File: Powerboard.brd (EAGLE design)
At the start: 87.5 x 150 mm, 9 parts

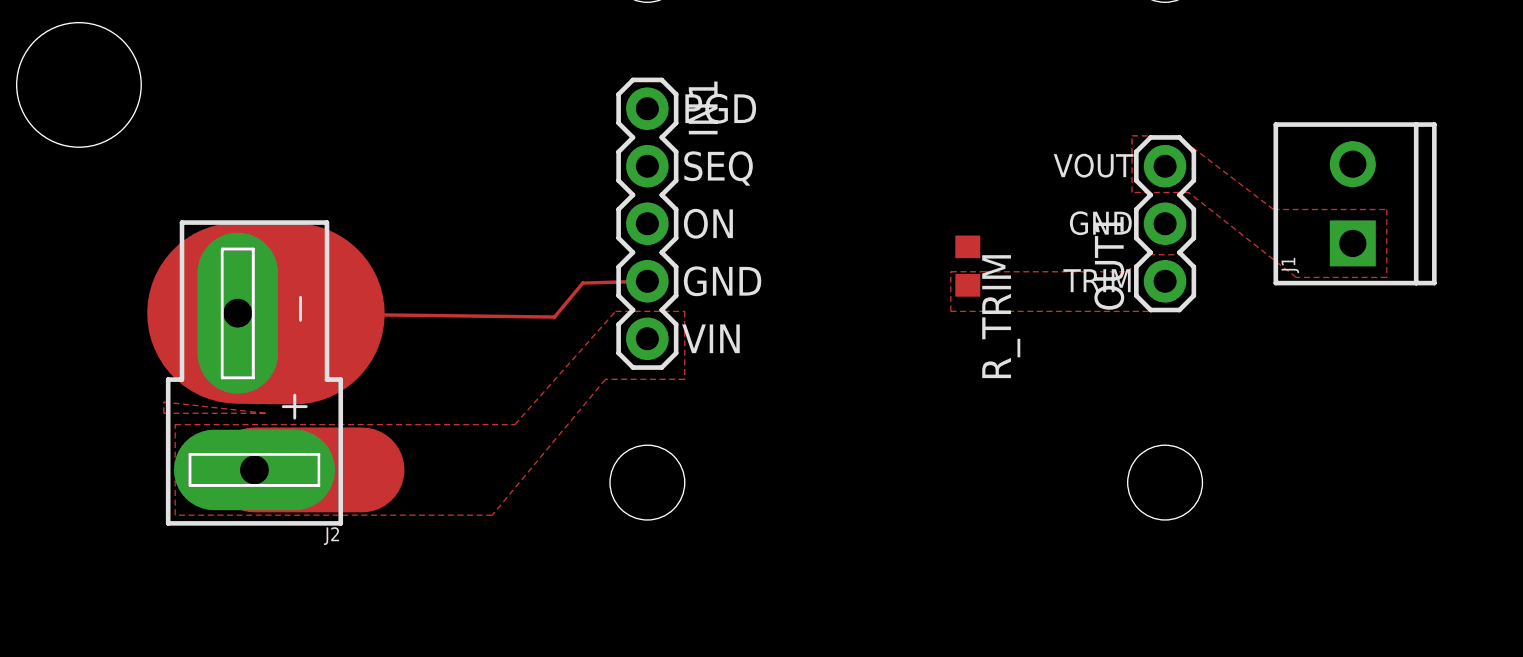
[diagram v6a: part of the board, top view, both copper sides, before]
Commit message: Rewire Powerboard
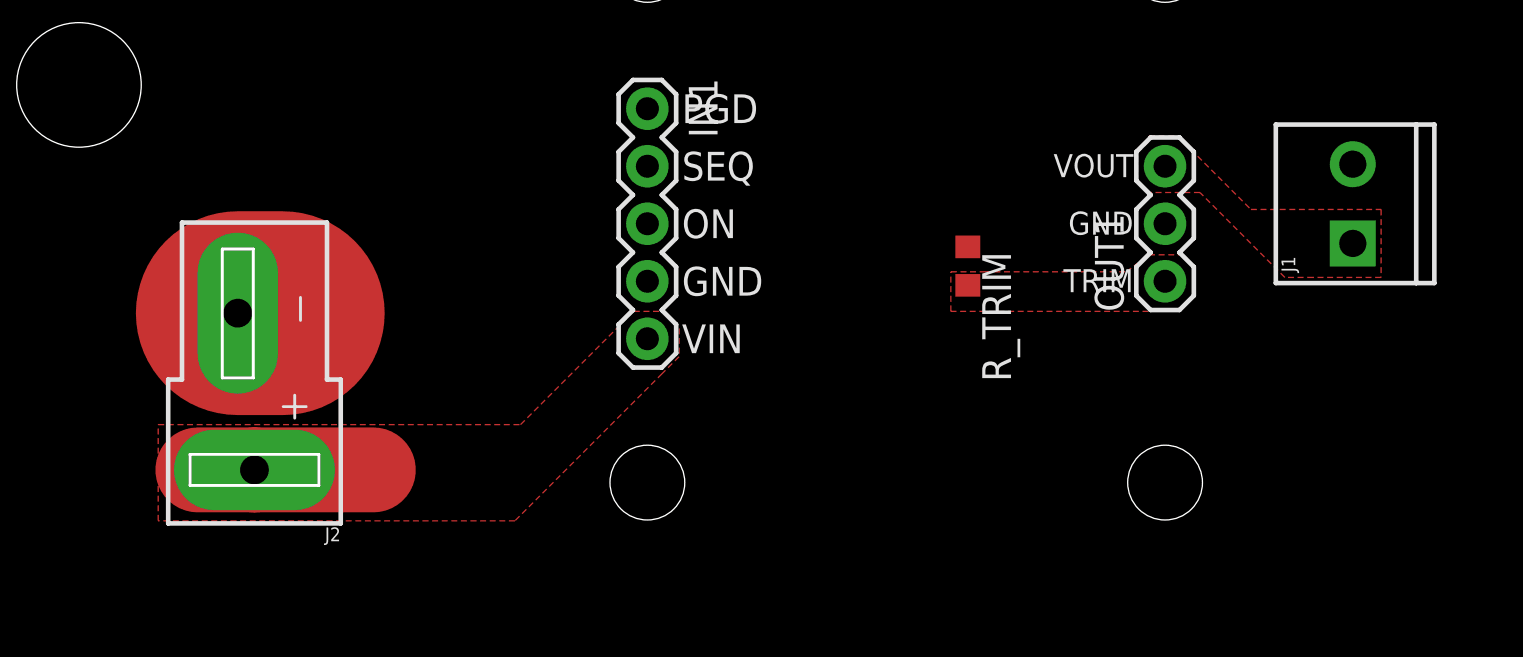
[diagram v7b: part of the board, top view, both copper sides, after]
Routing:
- net GND: track 18.8 -> 2.52 mm
- net VIN: track 4.75 -> 7.75 mm
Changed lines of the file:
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@@
 <?xml version="1.0" encoding="utf-8"?>
 <!DOCTYPE eagle SYSTEM "eagle.dtd">
-<eagle version="9.3.0">
+<eagle version="9.1.3">
 <drawing>
 <settings>
@@
 <hole x="77.75" y="140" drill="5.5"/>
 <dimension x1="77.75" y1="142.75" x2="77.75" y2="137.25" x3="97" y3="140" textsize="1.778" layer="47" dtype="diameter"/>
-<dimension x1="78" y1="140" x2="10" y2="140" x3="44" y3="169" textsize="1.778" layer="47" dtype="diameter"/>
+<dimension x1="78" y1="140" x2="10" y2="140" x3="44" y3="168.75" textsize="1.778" layer="47" dtype="diameter"/>
 <dimension x1="10" y1="9" x2="10" y2="139" x3="-10" y3="74" textsize="1.778" layer="47" dtype="diameter"/>
 <dimension x1="26" y1="150" x2="26" y2="0" x3="-15" y3="75" textsize="1.778" layer="47"/>
@@
 <contactref element="J2" pad="-"/>
 <contactref element="J1" pad="2"/>
-<polygon width="0.1524" layer="1" thermals="no">
-<vertex x="13.5" y="126"/>
-<vertex x="18" y="125.5"/>
-<vertex x="13.5" y="125.5"/>
-</polygon>
 <polygon width="0.1524" layer="1" thermals="no" rank="6">
 <vertex x="0" y="150"/>
@@
 <vertex x="87.5" y="150"/>
 </polygon>
-<wire x1="16.7634" y1="129.9215" x2="19.251728125" y2="129.8909875" width="8" layer="1"/>
-<wire x1="19.251728125" y1="129.8909875" x2="30.75" y2="129.75" width="0.1524" layer="1"/>
-<wire x1="30.75" y1="129.75" x2="32" y2="131.25" width="0.1524" layer="1"/>
-<wire x1="32" y1="131.25" x2="34.85" y2="131.33" width="0.1524" layer="1"/>
+<wire x1="16.7634" y1="129.9215" x2="18.75" y2="129.9215" width="9" layer="1"/>
+<wire x1="18.75" y1="129.9215" x2="19.1715" y2="129.9215" width="0.1524" layer="1"/>
+<wire x1="19.1715" y1="129.9215" x2="19.25" y2="130" width="0.1524" layer="1"/>
 </signal>
 <signal name="SEQ">
@@
 <contactref element="J2" pad="+"/>
 <polygon width="0.1524" layer="1" thermals="no">
-<vertex x="14" y="125"/>
-<vertex x="29" y="125"/>
-<vertex x="33.44444375" y="130"/>
-<vertex x="36.5" y="130"/>
-<vertex x="36.5" y="127"/>
-<vertex x="33" y="127"/>
-<vertex x="28" y="121"/>
-<vertex x="14" y="121"/>
+<vertex x="34.25" y="130"/>
+<vertex x="35.5" y="130"/>
+<vertex x="36" y="129.5"/>
+<vertex x="36.25" y="129.25"/>
+<vertex x="36.25" y="128"/>
+<vertex x="35.5" y="127.25"/>
+<vertex x="29" y="120.75"/>
+<vertex x="13.25" y="120.75"/>
+<vertex x="13.25" y="125"/>
+<vertex x="29.25" y="125"/>
 </polygon>
-<wire x1="17.5" y1="123" x2="22.25" y2="123" width="3.75" layer="1"/>
+<wire x1="17.5" y1="123" x2="22.75" y2="123" width="3.75" layer="1"/>
+<wire x1="17.5" y1="123" x2="15" y2="123" width="3.75" layer="1"/>
 </signal>
 <signal name="VOUT">
@@
 <contactref element="J1" pad="1"/>
 <polygon width="0.1524" layer="1" thermals="no">
-<vertex x="56.25" y="135.25"/>
-<vertex x="56.25" y="137.75"/>
+<vertex x="67.25" y="131.5"/>
+<vertex x="64.25" y="131.5"/>
+<vertex x="63" y="131.5"/>
+<vertex x="59.25" y="135.25"/>
+<vertex x="57" y="135.25"/>
+<vertex x="56.5" y="135.75"/>
+<vertex x="56.5" y="137"/>
+<vertex x="57" y="137.5"/>
+<vertex x="57" y="137.75"/>
 <vertex x="58.25" y="137.75"/>
-<vertex x="62.5" y="134.5"/>
-<vertex x="67.5" y="134.5"/>
-<vertex x="67.5" y="131.5"/>
-<vertex x="63.5" y="131.5"/>
-<vertex x="58.75" y="135.25"/>
+<vertex x="61.5" y="134.5"/>
+<vertex x="67.25" y="134.5"/>
 </polygon>
 </signal>
